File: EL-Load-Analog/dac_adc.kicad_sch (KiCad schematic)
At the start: 43 parts, among them U11 DAC8555, U12 DAC8555, U14 MCP6004, U18 MCP6V51, U19 MCP6V51, U20 ADS131M02

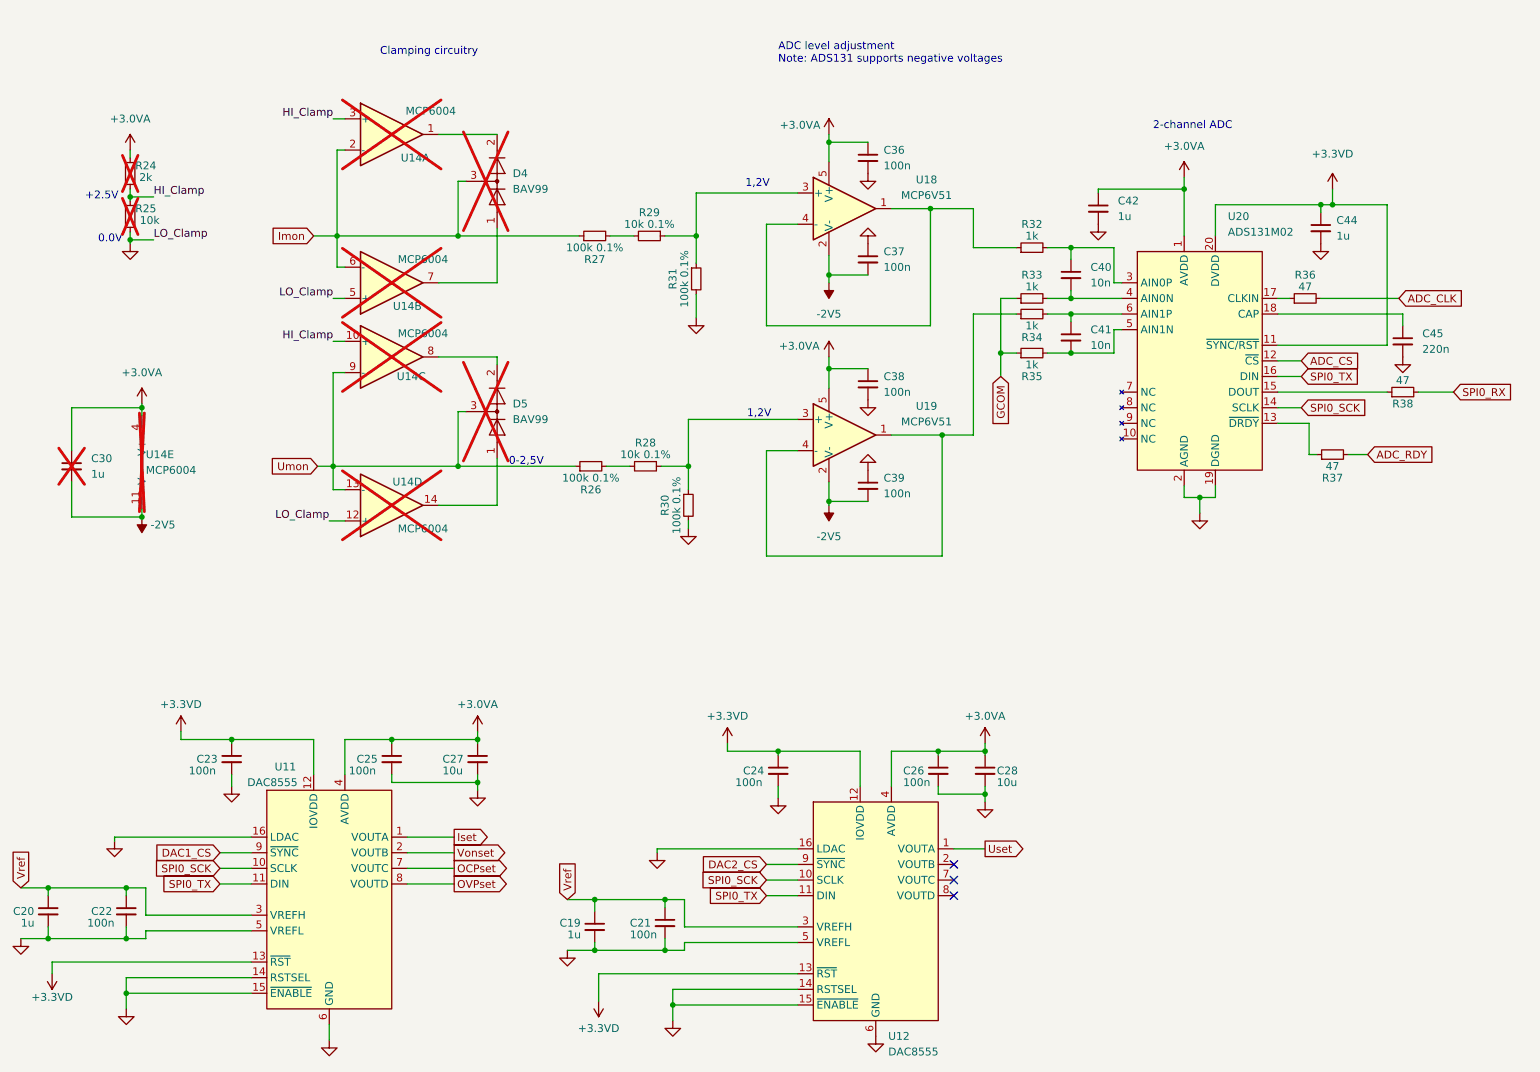
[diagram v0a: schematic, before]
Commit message: Added heatsink moutingholes, reverse polarity, moved snubbers.
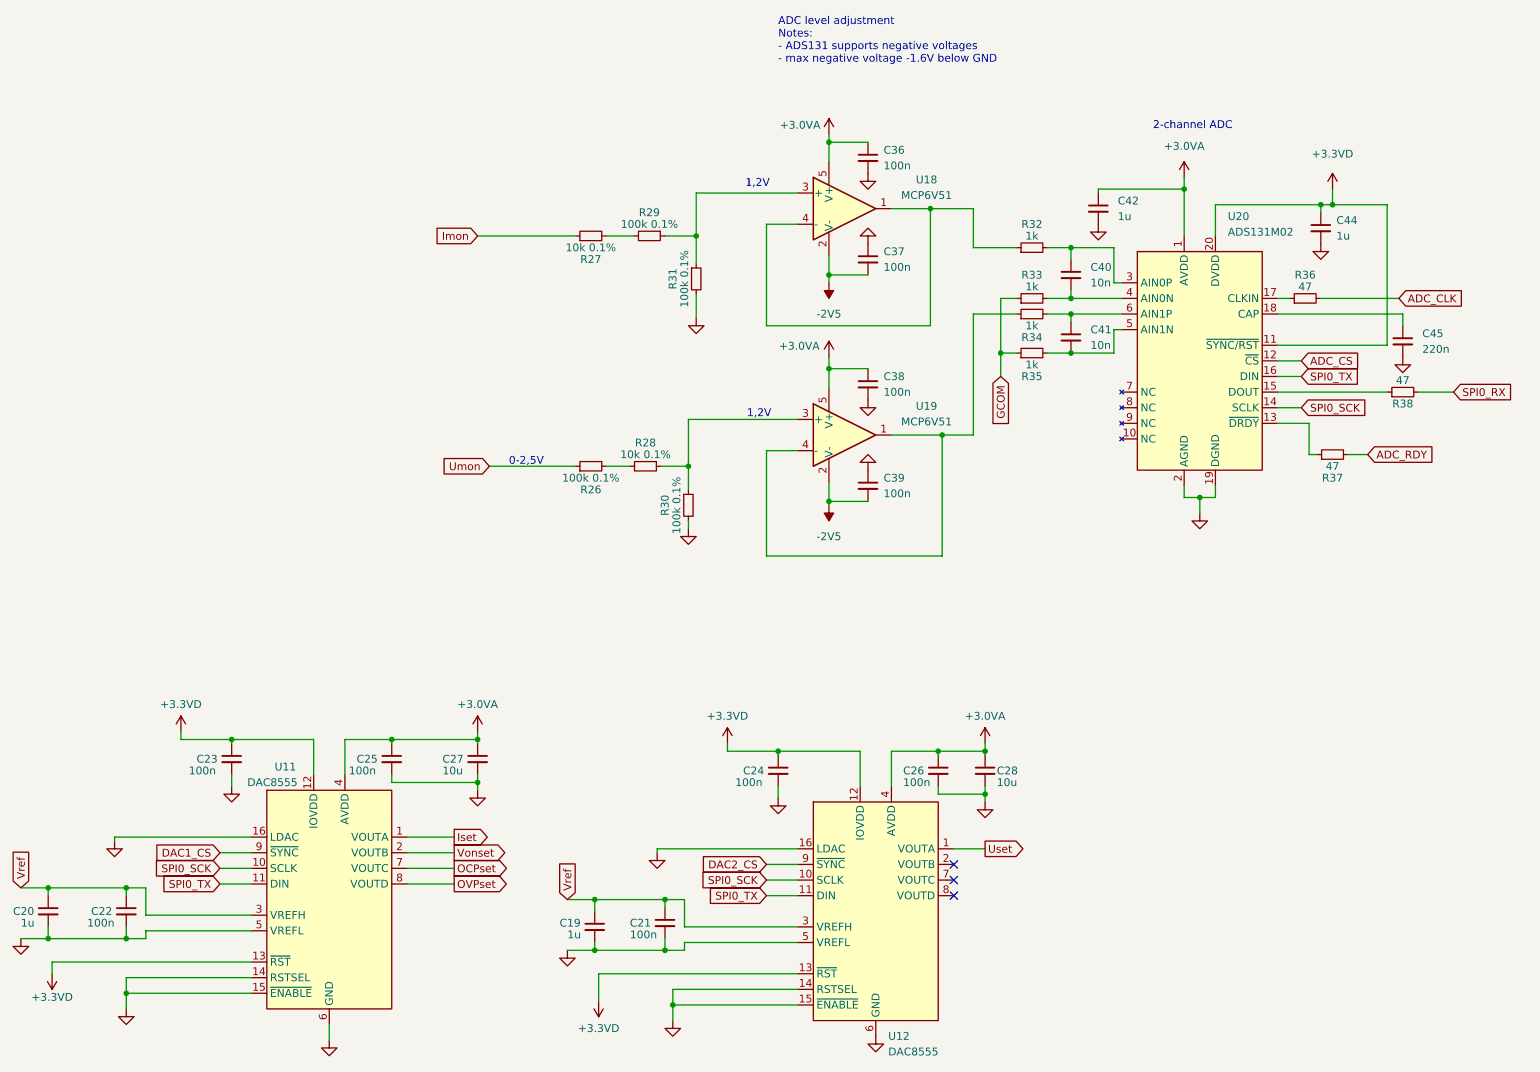
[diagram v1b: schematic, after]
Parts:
- removed C30: 1u, Capacitor_SMD:C_0805_2012Metric, symbol Device:C_Small
- removed D4, D5: BAV99, Package_TO_SOT_SMD:SOT-23, symbol Diode:BAV99
- removed R24: 2k, Resistor_SMD:R_0805_2012Metric, symbol Device:R_Small
- removed R25: 10k, Resistor_SMD:R_0805_2012Metric, symbol Device:R_Small
- removed U14: MCP6004, Package_SO:SOIC-14_3.9x8.7mm_P1.27mm, symbol Amplifier_Operational:MCP6004
- R27: value 100k 0.1% -> 10k 0.1%; Part Name R_100k_0805_0.1% -> R_10k_0805_0.1%
- R29: value 10k 0.1% -> 100k 0.1%; Part Name R_10k_0805_0.1% -> R_100k_0805_0.1%
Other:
- note added: "ADC level adjustment Notes: - ADS131 supports negative voltages - max negative voltage -1.6V below GND"
- note removed: "+2.5V"
- note removed: "0.0V"
- note removed: "ADC level adjustment Note: ADS131 supports negative voltages"
- note removed: "Clamping circuitry"
- moved on the sheet: R27

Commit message: v4 Analog board design. Features reverse polarity, remote sense error and new clamping circuitry.
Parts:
- C21, C22, C23, C24, C25, C26, C36, C37, C38, C39: Part Name C_100.0nF_0805_20% -> C_100.0nF_50V_0805_10%_X7R
- C27, C28: Part Name C_10.0uF_25V_X7R_10%_0805 -> C_10.0uF_25V_X5R_10%_0805
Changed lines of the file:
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@@
   (title_block
     (title "Electronic Load Analog Test Board")
-    (date "2024-02-06")
+    (date "2024-11-10")
     (rev "${VERSION}")
     (comment 1 "License: CERN-OHL-W-2.0")
@@
       (effects (font (size 1.27 1.27)) hide)
     )
-    (property "Part Name" "C_100.0nF_0805_20%" (at 154.305 80.01 0)
+    (property "Part Name" "C_100.0nF_50V_0805_10%_X7R " (at 154.305 80.01 0)
       (effects (font (size 1.27 1.27)) hide)
     )
@@
       (effects (font (size 1.27 1.27)) hide)
     )
-    (property "Part Name" "C_100.0nF_0805_20%" (at 76.835 140.97 0)
+    (property "Part Name" "C_100.0nF_50V_0805_10%_X7R " (at 76.835 140.97 0)
       (effects (font (size 1.27 1.27)) hide)
     )
@@
       (effects (font (size 1.27 1.27)) hide)
     )
-    (property "Part Name" "C_100.0nF_0805_20%" (at 121.285 167.64 0)
+    (property "Part Name" "C_100.0nF_50V_0805_10%_X7R " (at 121.285 167.64 0)
       (effects (font (size 1.27 1.27)) hide)
     )
@@
       (effects (font (size 1.27 1.27)) hide)
     )
-    (property "Part Name" "C_10.0uF_25V_X7R_10%_0805" (at 173.355 142.875 0)
+    (property "Part Name" "C_10.0uF_25V_X5R_10%_0805" (at 173.355 142.875 0)
       (effects (font (size 1.27 1.27)) hide)
     )
@@
       (effects (font (size 1.27 1.27)) hide)
     )
-    (property "Part Name" "C_100.0nF_0805_20%" (at 154.305 43.18 0)
+    (property "Part Name" "C_100.0nF_50V_0805_10%_X7R " (at 154.305 43.18 0)
       (effects (font (size 1.27 1.27)) hide)
     )
@@
       (effects (font (size 1.27 1.27)) hide)
     )
-    (property "Part Name" "C_100.0nF_0805_20%" (at 50.8 140.97 0)
+    (property "Part Name" "C_100.0nF_50V_0805_10%_X7R " (at 50.8 140.97 0)
       (effects (font (size 1.27 1.27)) hide)
     )
@@
       (effects (font (size 1.27 1.27)) hide)
     )
-    (property "Part Name" "C_100.0nF_0805_20%" (at 33.655 165.735 0)
+    (property "Part Name" "C_100.0nF_50V_0805_10%_X7R " (at 33.655 165.735 0)
       (effects (font (size 1.27 1.27)) hide)
     )
@@
       (effects (font (size 1.27 1.27)) hide)
     )
-    (property "Part Name" "C_100.0nF_0805_20%" (at 139.7 142.875 0)
+    (property "Part Name" "C_100.0nF_50V_0805_10%_X7R " (at 139.7 142.875 0)
       (effects (font (size 1.27 1.27)) hide)
     )
@@
       (effects (font (size 1.27 1.27)) hide)
     )
-    (property "Part Name" "C_10.0uF_25V_X7R_10%_0805" (at 90.805 140.97 0)
+    (property "Part Name" "C_10.0uF_25V_X5R_10%_0805" (at 90.805 140.97 0)
       (effects (font (size 1.27 1.27)) hide)
     )
@@
       (effects (font (size 1.27 1.27)) hide)
     )
-    (property "Part Name" "C_100.0nF_0805_20%" (at 154.305 96.52 0)
+    (property "Part Name" "C_100.0nF_50V_0805_10%_X7R " (at 154.305 96.52 0)
       (effects (font (size 1.27 1.27)) hide)
     )
@@
       (effects (font (size 1.27 1.27)) hide)
     )
-    (property "Part Name" "C_100.0nF_0805_20%" (at 165.735 142.875 0)
+    (property "Part Name" "C_100.0nF_50V_0805_10%_X7R " (at 165.735 142.875 0)
       (effects (font (size 1.27 1.27)) hide)
     )
@@
       (effects (font (size 1.27 1.27)) hide)
     )
-    (property "Part Name" "C_100.0nF_0805_20%" (at 154.305 59.69 0)
-      (effects (font (size 1.27 1.27)) hide)
-    )
+    (property "Part Name" "C_100.0nF_50V_0805_10%_X7R " (at 154.305 59.69 0)
+      (effects (font (size 1.27 1.27)) hide)
+    )
